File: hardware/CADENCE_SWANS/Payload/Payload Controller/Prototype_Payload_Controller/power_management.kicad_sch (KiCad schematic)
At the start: 37 parts, among them U6 LT8612, U7 LT8612

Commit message: minor updates
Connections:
- net +1V8: no longer C13.1, U5.10 (OUTS), U5.11 (OUT), U5.12 (OUT)
- new net +1V2: C13.1, U5.10 (OUTS), U5.11 (OUT), U5.12 (OUT)
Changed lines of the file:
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@@
 		(on_board yes)
 		(dnp no)
-		(fields_autoplaced yes)
 		(property "Reference" "#PWR028"
 			(at 346.71 171.45 0)
@@
 			)
 		)
-		(property "Value" "+1V8"
-			(at 346.71 162.56 0)
+		(property "Value" "+1V2"
+			(at 343.916 163.068 0)
 			(effects
 				(font
 					(size 1.27 1.27)
 				)
+				(justify left)
 			)
 		)

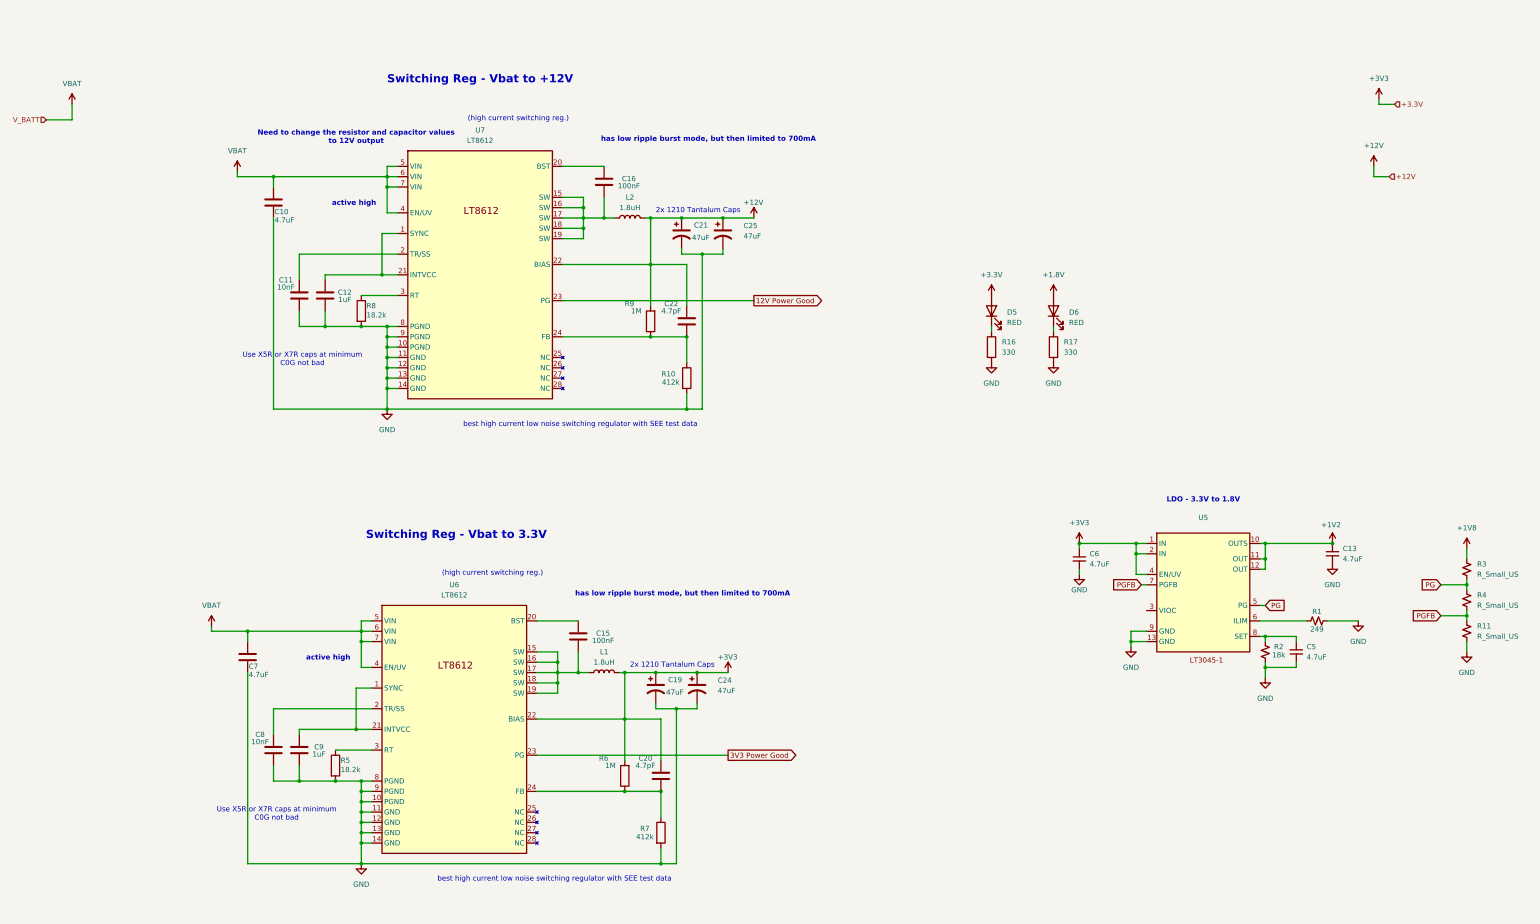
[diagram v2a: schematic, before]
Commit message: identified debug and usb pins
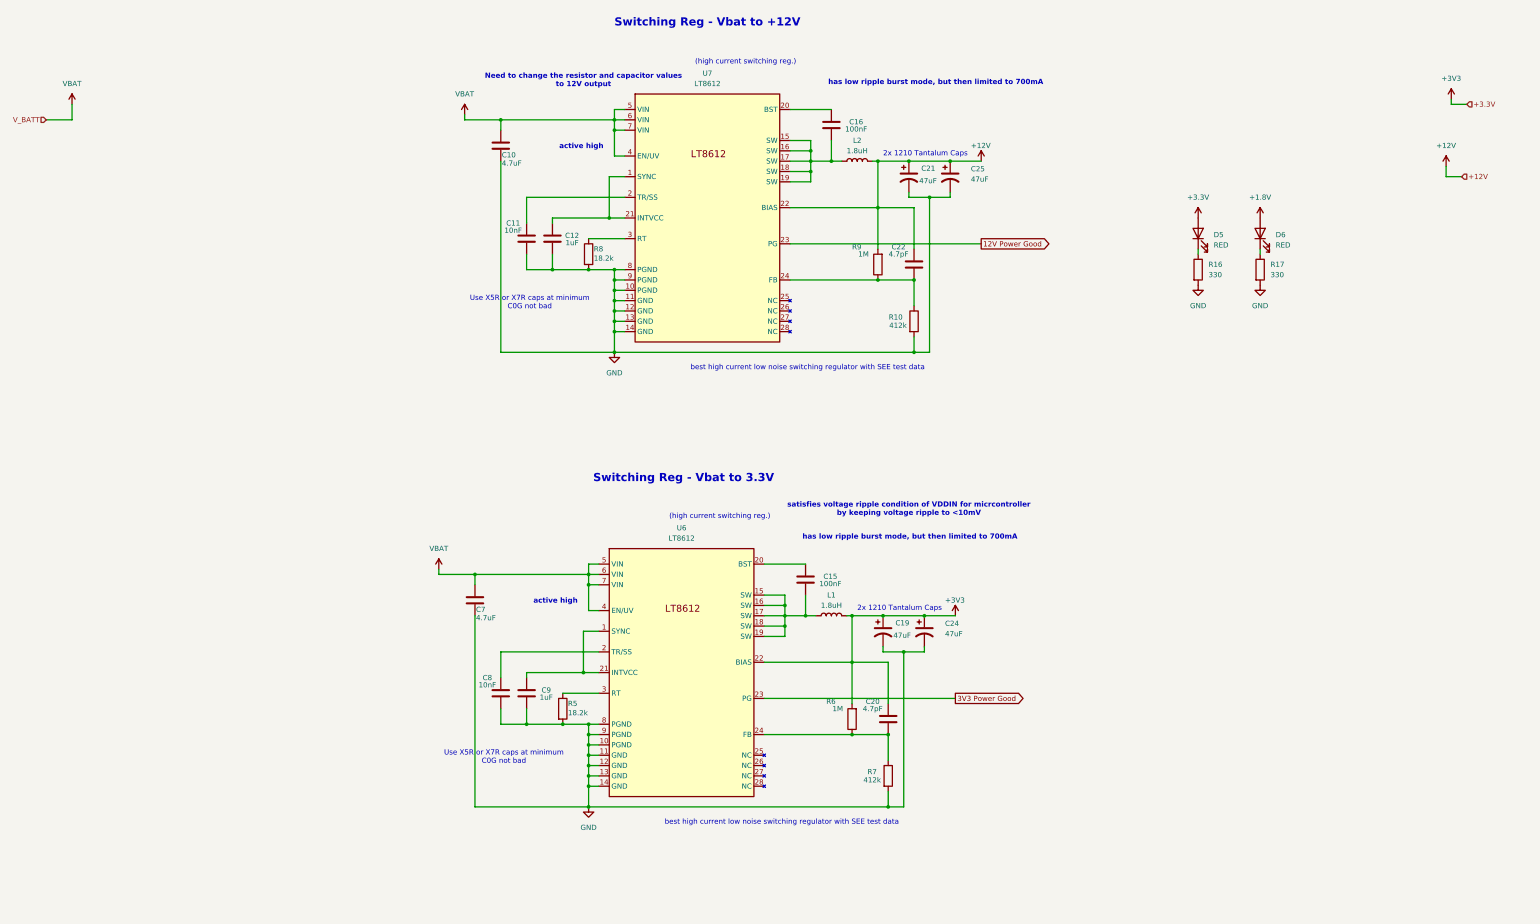
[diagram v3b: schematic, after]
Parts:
- removed C13, C5, C6: 4.7uF, symbol Device:C_Small
- removed R1: 249, symbol Device:R_Small_US
- removed R11, R3, R4: R_Small_US, symbol Device:R_Small_US
- removed R2: 18k, symbol Device:R_Small_US
- removed U5: ~, symbol Payload_Controller_EM:LT3045-1
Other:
- note added: "satisfies voltage ripple condition of VDDIN for micrcontroller by keeping voltage ripple to <10mV"
- note removed: "LDO - 3.3V to 1.8V"
- moved on the sheet: C10, C11, C12, C15, C16, C19, C20, C21, C22, C24, C25, C7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

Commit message: updated power regulators
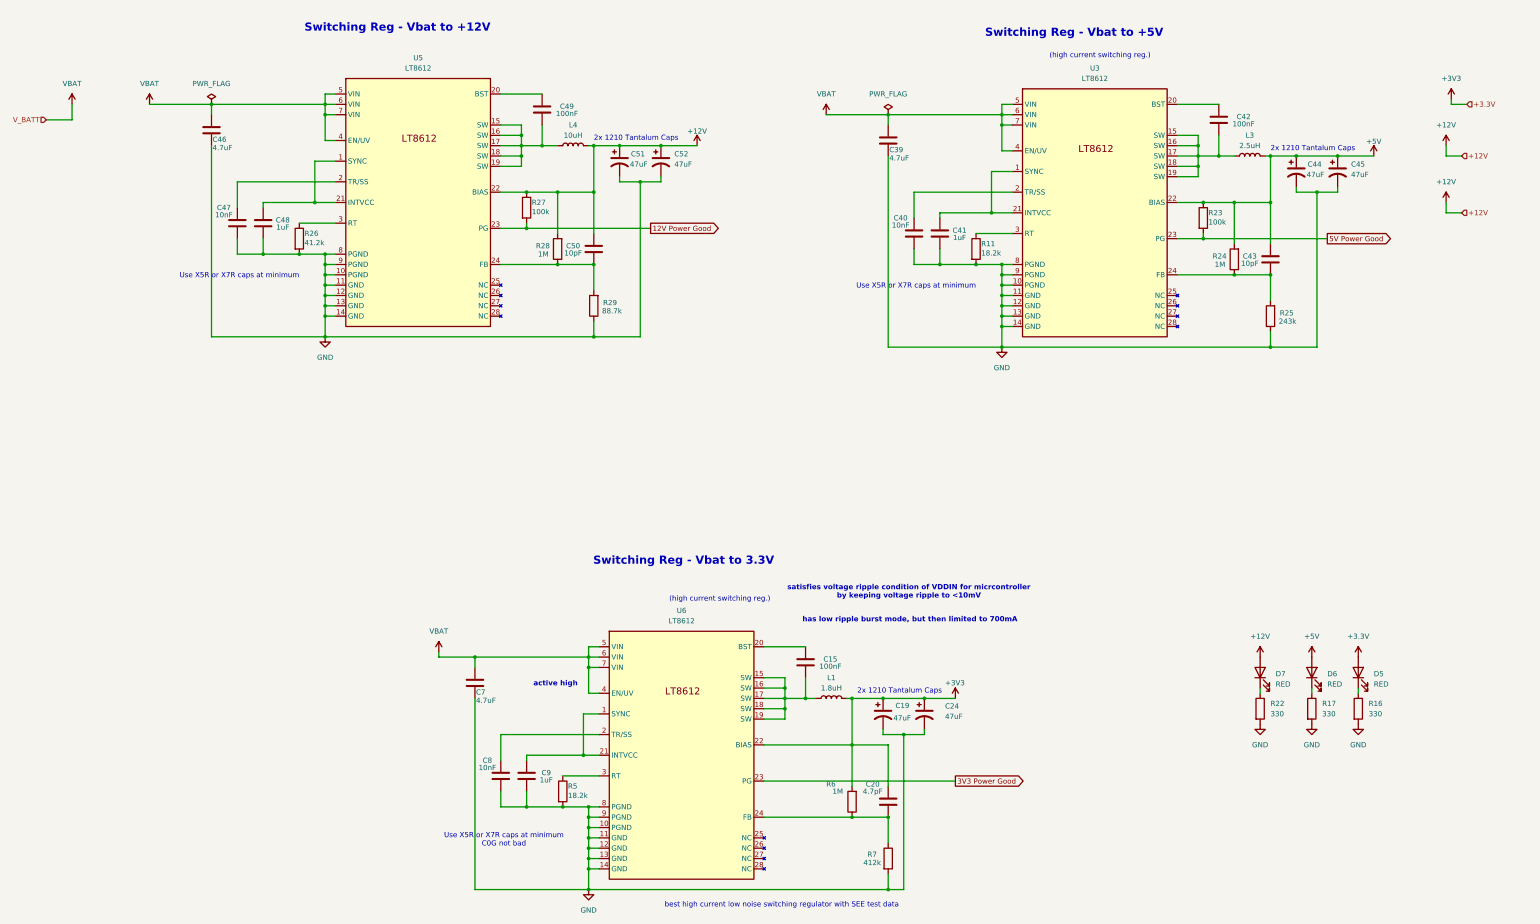
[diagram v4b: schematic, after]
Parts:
- removed C10: 4.7uF, Capacitor_SMD:C_0603_1608Metric, symbol Device:C
- removed C11: 10nF, Capacitor_SMD:C_0603_1608Metric, symbol Device:C
- removed C12: 1uF, Capacitor_SMD:C_0603_1608Metric, symbol Device:C
- removed C16: 100nF, Capacitor_SMD:C_0603_1608Metric, symbol Device:C
- removed C21, C25: 47uF, symbol Device:C_Polarized_US
- removed C22: 4.7pF, Capacitor_SMD:C_0603_1608Metric, symbol Device:C
- removed L2: 1.8uH, symbol Device:L
- removed R10: 412k, Resistor_SMD:R_0402_1005Metric, symbol Device:R
- removed R8: 18.2k, Resistor_SMD:R_0402_1005Metric, symbol Device:R
- removed R9: 1M, Resistor_SMD:R_0402_1005Metric, symbol Device:R
- removed U7: LT8612, LT8612:QFN-28_UDE_LTI, symbol cadence carrier custom symbols:LT8612
- added C39, C46: 4.7uF, Capacitor_SMD:C_0603_1608Metric, symbol Device:C
- added C40, C47: 10nF, Capacitor_SMD:C_0402_1005Metric, symbol Device:C
- added C41, C48: 1uF, Capacitor_SMD:C_0603_1608Metric, symbol Device:C
- added C42, C49: 100nF, Capacitor_SMD:C_0402_1005Metric, symbol Device:C
- added C43, C50: 10pF, Capacitor_SMD:C_0402_1005Metric, symbol Device:C
- added C44, C45, C51, C52: 47uF, Capacitor_SMD:C_0805_2012Metric, symbol Device:C_Polarized_US
- added D7: RED, LED_SMD:LED_0603_1608Metric, symbol Device:LED
- added L3: 2.5uH, Footprints:IND-SMD_L10.9-W10.0, symbol Device:L
- added L4: 10uH, Footprints:IND-SMD_L10.9-W10.0, symbol Device:L
- added R11: 18.2k, Resistor_SMD:R_0402_1005Metric, symbol Device:R
- added R22: 330, Resistor_SMD:R_0402_1005Metric, symbol Device:R
- added R23, R27: 100k, Resistor_SMD:R_0402_1005Metric, symbol Device:R
- added R24, R28: 1M, Resistor_SMD:R_0603_1608Metric, symbol Device:R
- added R25: 243k, Resistor_SMD:R_0402_1005Metric, symbol Device:R
- added R26: 41.2k, Resistor_SMD:R_0402_1005Metric, symbol Device:R
- added R29: 88.7k, Resistor_SMD:R_0402_1005Metric, symbol Device:R
- added U3, U5: LT8612, LT8612:QFN-28_UDE_LTI, symbol cadence carrier custom symbols:LT8612
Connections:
- net +12V: now also C50.2, C51.1, C52.1, D7.2 (A), L4.2, R27.1, R28.2, U5.22 (BIAS)
- net 12V Power Good: now also R27.2, U5.23 (PG)
- net GND: now also C39.2, C40.1, C41.1, C44.2, C45.2, C46.2, C47.1, C48.1, C51.2, C52.2, R11.2, R22.2, R25.1, R26.2, R29.1, U3.10 (PGND), U3.11 (GND), U3.12 (GND), U3.13 (GND), U3.14 (GND), U3.8 (PGND), U3.9 (PGND), U5.10 (PGND), U5.11 (GND), U5.12 (GND), U5.13 (GND), U5.14 (GND), U5.8 (PGND), U5.9 (PGND)
- net VBAT: now also C39.1, C46.1, U3.4 (EN/UV), U3.5 (VIN), U3.6 (VIN), U3.7 (VIN), U5.4 (EN/UV), U5.5 (VIN), U5.6 (VIN), U5.7 (VIN)
- net +1.8V renamed +5V
- net +5V: now also C43.2, C44.1, C45.1, L3.2, R23.1, R24.2, U3.22 (BIAS)
- new net: D7.1 (K), R22.1
- new net: C47.2, U5.2 (TR/SS)
- new net: C48.2, U5.1 (SYNC), U5.21 (INTVCC)
- new net: C43.1, R24.1, R25.2, U3.24 (FB)
- new net: C49.1, L4.1, U5.15 (SW), U5.16 (SW), U5.17 (SW), U5.18 (SW), U5.19 (SW)
- new net: C42.1, L3.1, U3.15 (SW), U3.16 (SW), U3.17 (SW), U3.18 (SW), U3.19 (SW)
- new net: C42.2, U3.20 (BST)
- new net: C40.2, U3.2 (TR/SS)
- new net: C50.1, R28.1, R29.2, U5.24 (FB)
- new net: C41.2, U3.1 (SYNC), U3.21 (INTVCC)
- new net: R26.1, U5.3 (RT)
- new net: R11.1, U3.3 (RT)
- new net: C49.2, U5.20 (BST)
- new net 5V Power Good: R23.2, U3.23 (PG)
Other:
- note added: "Switching Reg - Vbat to +5V"
- note added: "Use X5R or X7R caps at minimum"
- note removed: "Need to change the resistor and capacitor values to 12V output"
- moved on the sheet: C15, C19, C20, C24, C7, C8, C9, D5, D6, L1, R16, R17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

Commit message: cleaned up schematics and assigned footprints for resistors and capacitors
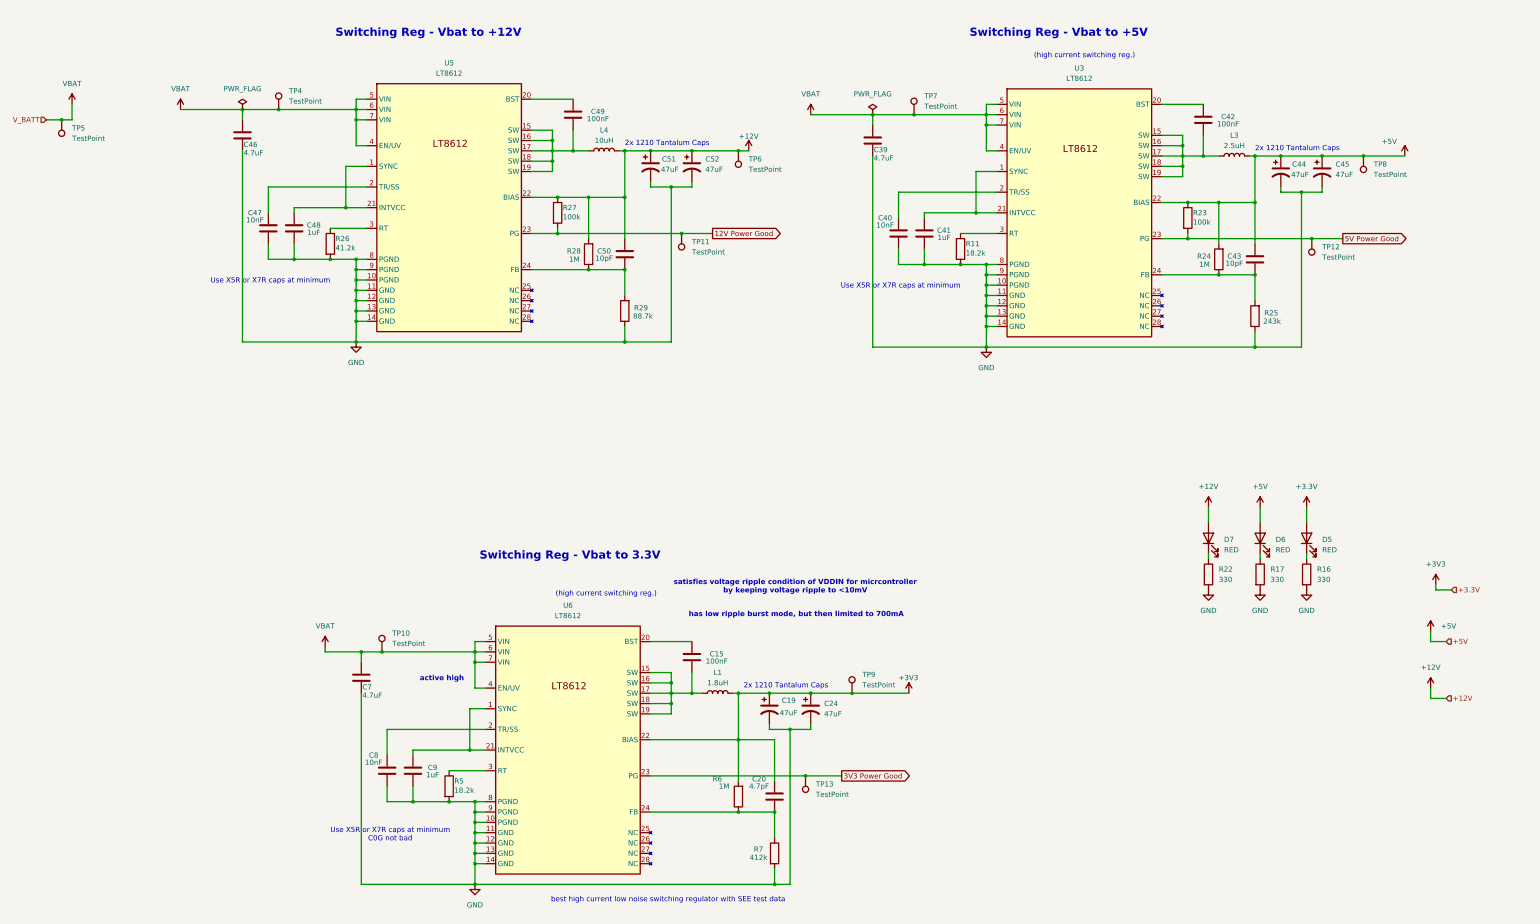
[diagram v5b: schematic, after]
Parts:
- added TP10, TP11, TP12, TP13, TP4, TP5, TP6, TP7, TP8, TP9: TestPoint, TestPoint:TestPoint_Pad_1.0x1.0mm, symbol Connector:TestPoint
- C19, C24: footprint (none) -> Capacitor_SMD:C_0603_1608Metric
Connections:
- net +12V: now also TP6.1
- net +3.3V: now also TP9.1
- net +5V: now also TP8.1
- net 12V Power Good: now also TP11.1
- net 3V3 Power Good: now also TP13.1
- net 5V Power Good: now also TP12.1
- net VBAT: now also TP10.1, TP4.1, TP5.1, TP7.1
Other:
- moved on the sheet: C15, C19, C20, C24, C39, C40, C41, C42, C43, C44, C45, C46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

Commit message: updates
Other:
- moved on the sheet: C15, C19, C20, C24, C39, C40, C41, C42, C43, C44, C45, C46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

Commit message: linked more footprints
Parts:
- L1: footprint (none) -> Footprints:IND-SMD_L10.9-W10.0
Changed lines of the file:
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@@
 			)
 		)
-		(property "Footprint" ""
+		(property "Footprint" "Footprints:IND-SMD_L10.9-W10.0"
 			(at 214.63 198.12 0)
 			(effects

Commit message: resolved ERC errors
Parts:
- added C105: 100nF, Capacitor_SMD:C_0603_1608Metric, symbol Device:C
- added R121: 0.002, Resistor_SMD:R_0402_1005Metric, symbol Device:R
- added U31: INA219AxDCN, Package_TO_SOT_SMD:SOT-23-8, symbol Sensor_Energy:INA219AxDCN
- L1, L3, L4: footprint Footprints:IND-SMD_L10.9-W10.0 -> Inductor_SMD:L_6.3x6.3_H3
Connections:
- net +3.3V: now also R121.2, U31.2 (IN-); no longer C19.1, C20.2, C24.1, L1.2, R6.2, TP9.1, U6.22 (BIAS)
- net GND: now also C105.2, U31.3 (GND), U31.7 (A0), U31.8 (A1)
- net VBAT: now also C105.1, R121.1, U31.1 (IN+), U31.4 (VS)
- new net +3V3: C19.1, C20.2, C24.1, L1.2, R6.2, TP9.1, U6.22 (BIAS)
- new net I2C0_SCL: U31.5 (SCL)
- new net I2C0_SDA: U31.6 (SDA)
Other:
- note added: "Board Power Monitor"
- note added: "I2C Address: 1000000"
- note added: "Use high watt shunt!"
- moved on the sheet: C15, C19, C20, C24, C7, C8, C9, D5, D6, D7, L1, R16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
